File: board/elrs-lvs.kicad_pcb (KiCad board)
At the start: 4 copper layers, 46 x 22 mm, 150 parts, among them J1 PWM, J10 CF/Prog, J11 Holes, J12 Balance, J13 U.FL, J2 PWM, J3 PWM, J4 PWM, J5 PWM, J6 PWM, J7 PWM, J8 PWM, J9 Little Tower, SW1 SW_SPST, SW2 SW_SPST, U1 ESP32-PICO-V3, U2 SX1281, U3 TPSM82901SISR, U4 2450FM07D0034T, Y1 52Mhz TCXO

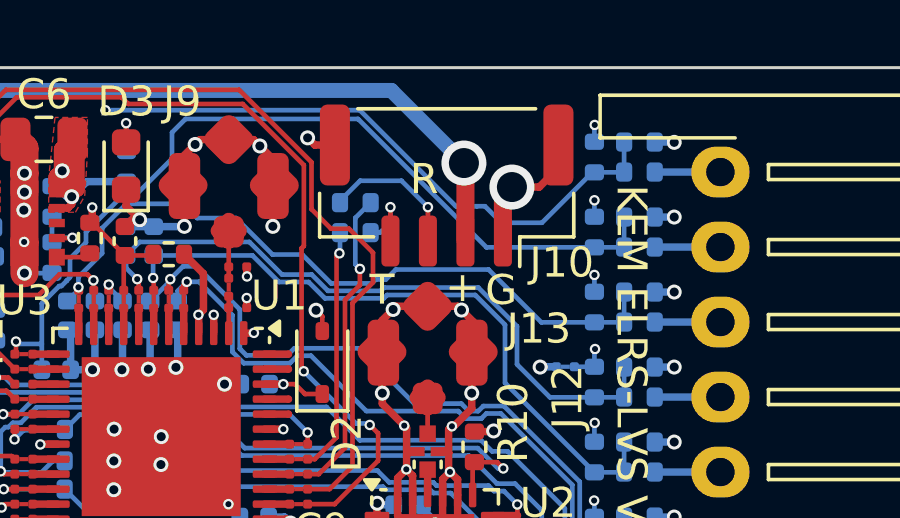
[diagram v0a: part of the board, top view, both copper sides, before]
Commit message: invert serial connector pinout
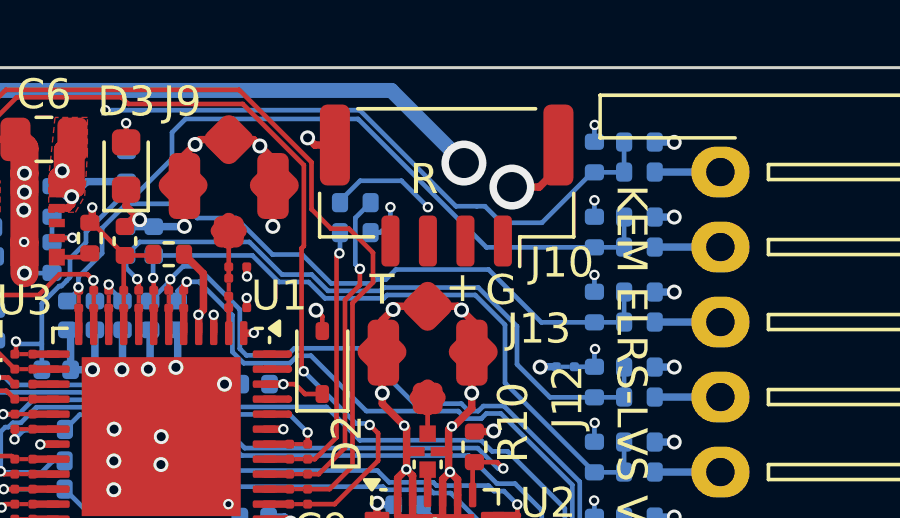
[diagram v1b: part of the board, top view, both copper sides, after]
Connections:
- J10 pad 1: GND -> Net-(J10-Pin_1)
- J10 pad 2: +5V -> Net-(J10-Pin_2)
- J10 pad 3: Net-(J10-Pin_3) -> +5V
- J10 pad 4: Net-(J10-Pin_4) -> GND
- R47 pad 1: Net-(J10-Pin_3) -> Net-(J10-Pin_2)
- R48 pad 1: Net-(J10-Pin_4) -> Net-(J10-Pin_1)
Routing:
- net Net-(J10-Pin_3): track 4.76 -> 0.00 mm, vias 1 -> 0
- net Net-(J10-Pin_2): track 0.00 -> 3.63 mm, vias 0 -> 1
- net +5V: track 150.8 -> 148.2 mm
- net Net-(J10-Pin_4): track 2.43 -> 0.00 mm, vias 1 -> 0
- net GND: track 300.4 -> 298.9 mm
- net Net-(J10-Pin_1): track 0.00 -> 1.30 mm, vias 0 -> 1

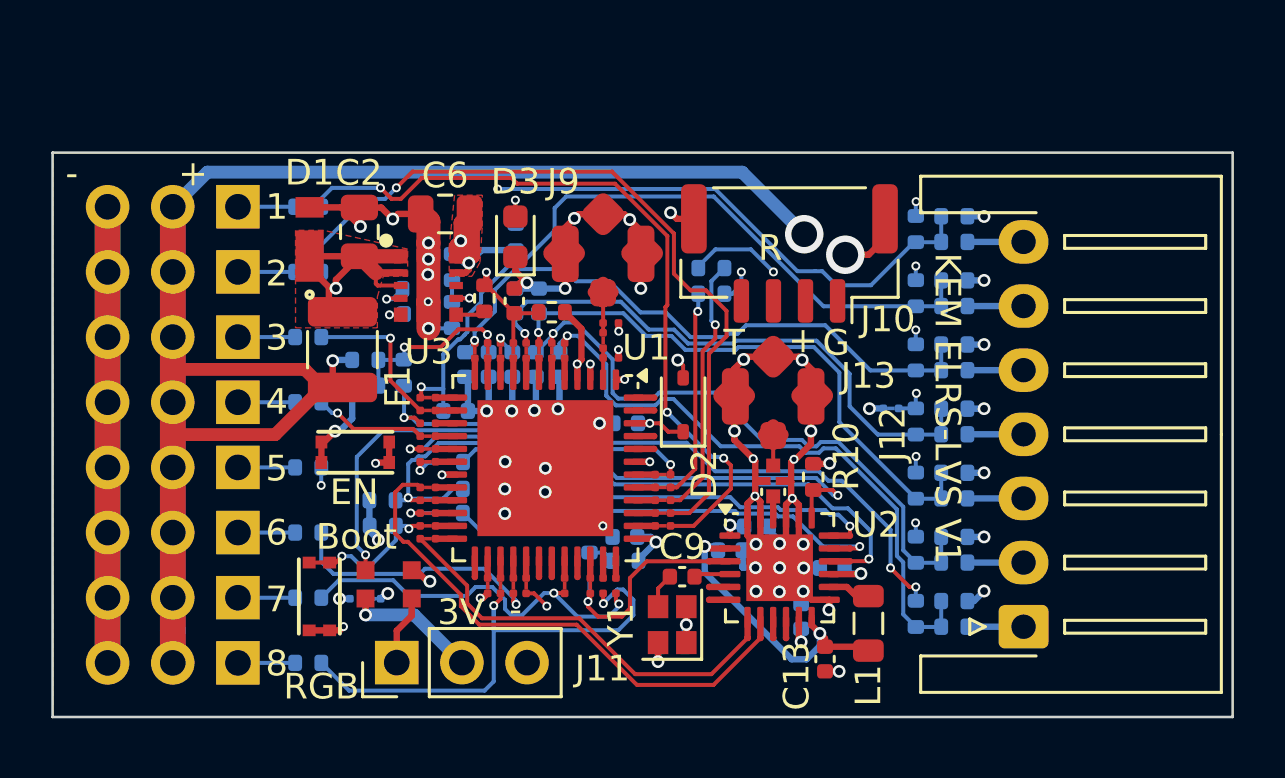
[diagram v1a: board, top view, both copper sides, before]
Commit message: remove dnp options and test points
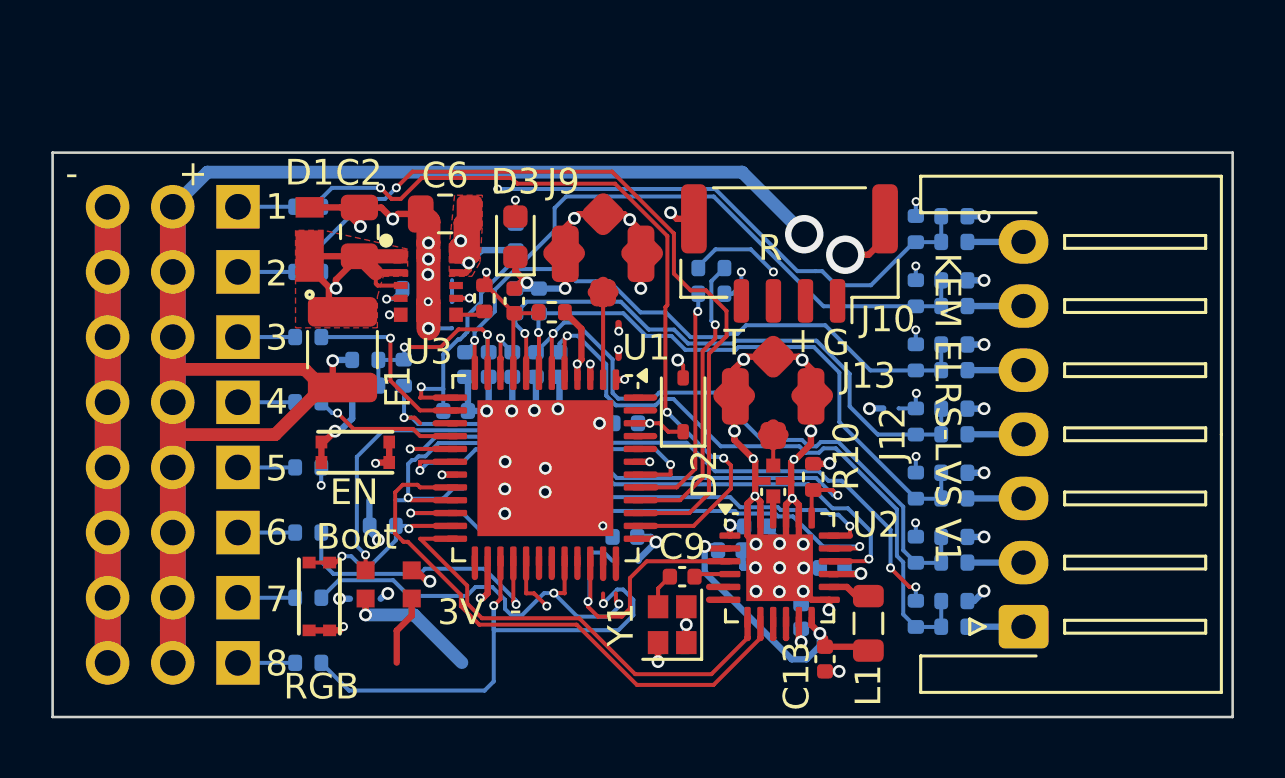
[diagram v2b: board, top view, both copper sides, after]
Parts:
- removed C22, C23: DNP, elrs-lvs:R_0201_0603_NP
- removed C5: DNP, Capacitor_SMD:C_0402_1005Metric
- removed J11: Holes, Connector_PinHeader_2.54mm:PinHeader_1x03_P2.54mm_Vertical
- removed JP1, JP12, JP13, JP14, JP15, JP16, JP17, JP18, JP19, JP2, JP20, JP21, JP22, JP23, JP25, JP26, JP27, JP29, JP3, JP31, JP32, JP33, JP34, JP35, JP36, JP4, JP41, JP5, JP7, JP8, L2: JP, elrs-lvs:R_0201_0603_JP
- removed JP24, JP28, JP30: NP, elrs-lvs:R_0201_0603_NP
- removed JP37: SolderJumper_3_Bridged12, elrs-lvs:R_0201_0603_JP_123
- removed R11, R12, R4, R5, R6, R7, R8, R9: DNP, Resistor_SMD:R_0402_1005Metric
- removed TP10, TP11, TP12, TP13, TP14, TP15, TP16, TP18, TP19, TP2, TP20, TP3, TP4, TP5, TP6, TP7, TP8, TP9: TP, elrs-lvs:TestPoint_Pad_D0.25mm
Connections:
- D4 pad 4: /LEDPWR -> +3.3V
- R31 pad 2: /VBAT_DET -> +3.3V
- R32 pad 2: /VBAT_DET -> +3.3V
- R33 pad 2: /VBAT_DET -> +3.3V
- R34 pad 2: /VBAT_DET -> +3.3V
- R35 pad 2: /VBAT_DET -> +3.3V
- R36 pad 2: /VBAT_DET -> +3.3V
- R37 pad 2: /VBAT_DET -> +3.3V
- R38 pad 2: /VBAT_DET -> +3.3V
- U1 pad 10: Net-(JP34-A) -> /LVS7
- U1 pad 11: Net-(JP35-A) -> /VS_5V
- U1 pad 12: Net-(JP32-A) -> /LVS5
- U1 pad 13: Net-(JP33-A) -> /LVS6
- U1 pad 14: Net-(JP29-A) -> /PWM3
- U1 pad 15: Net-(JP30-A) -> unconnected-(U1-IO26-Pad15)
- U1 pad 16: Net-(JP31-A) -> /PWM4
- U1 pad 17: Net-(JP22-A) -> /RADIO_NSS
- U1 pad 18: Net-(JP20-A) -> /RADIO_SCK
- U1 pad 2: Net-(U1-LNA_IN) -> Net-(J9-In)
- U1 pad 20: Net-(JP21-A) -> /RADIO_DIO1
- U1 pad 21: Net-(JP23-A) -> /RADIO_MISO
- U1 pad 22: Net-(JP14-A) -> /RADIO_MOSI
- U1 pad 23: Net-(JP12-A) -> /BOOT
- U1 pad 24: Net-(JP16-A) -> /RADIO_BUSY
- U1 pad 25: Net-(U1-IO16) -> unconnected-(U1-IO16-Pad25)
- U1 pad 26: Net-(JP36-A) -> +3.3V
- U1 pad 27: Net-(JP7-B) -> /PWM8
- U1 pad 28: Net-(JP18-A) -> /PWM6
- U1 pad 29: Net-(JP19-A) -> /PWM5
- U1 pad 30: Net-(U1-CMD) -> unconnected-(U1-CMD-Pad30)
- U1 pad 31: Net-(U1-CLK) -> unconnected-(U1-CLK-Pad31)
- U1 pad 32: Net-(JP8-B) -> /PWM7
- U1 pad 33: Net-(U1-SD1) -> unconnected-(U1-SD1-Pad33)
- U1 pad 34: Net-(JP17-A) -> /RADIO_RST
- U1 pad 35: Net-(JP24-A) -> unconnected-(U1-IO18-Pad35)
- U1 pad 36: Net-(JP28-A) -> unconnected-(U1-IO23-Pad36)
- U1 pad 38: Net-(JP25-A) -> /PWM1
- U1 pad 39: Net-(JP27-A) -> /PWM2
- U1 pad 40: Net-(JP15-A) -> /SERIAL_RX
- U1 pad 41: Net-(JP13-A) -> /SERIAL_TX
- U1 pad 42: Net-(JP26-A) -> /LED_RGB
- U1 pad 44: Net-(U1-XTAL_N_NC) -> unconnected-(U1-XTAL_N_NC-Pad44)
- U1 pad 45: Net-(U1-XTAL_P_NC) -> unconnected-(U1-XTAL_P_NC-Pad45)
- U1 pad 47: Net-(U1-CAP2_NC) -> unconnected-(U1-CAP2_NC-Pad47)
- U1 pad 48: Net-(U1-CAP1_NC) -> unconnected-(U1-CAP1_NC-Pad48)
- U1 pad 5: Net-(JP1-B) -> /LVS1
- U1 pad 6: Net-(JP2-B) -> /LVS2
- U1 pad 7: Net-(JP3-B) -> /LVS3
- U1 pad 8: Net-(JP4-B) -> /LVS4
- U1 pad 9: Net-(JP5-B) -> /RESET
- U2 pad 10: Net-(U2-DIO3) -> unconnected-(U2-DIO3-Pad10)
- U2 pad 5: Net-(TP9-Pad1) -> unconnected-(U2-GND-Pad5)
- U2 pad 6: Net-(U2-XTB) -> unconnected-(U2-XTB-Pad6)
- U2 pad 9: Net-(U2-DIO2) -> unconnected-(U2-DIO2-Pad9)
- U3 pad 5: Net-(U3-SS/TR) -> unconnected-(U3-SS/TR-Pad5)
- U3 pad 7: Net-(U3-FB) -> unconnected-(U3-FB-Pad7)
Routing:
- net +3.3V: track 98.8 -> 151.3 mm, vias 17 -> 27
- net /VBAT_DET: track 45.2 -> 0.00 mm, vias 9 -> 0
- net /LEDPWR: track 5.80 -> 0.00 mm, vias 1 -> 0
- net unconnected-(U3-FB-Pad7): track 0.00 -> 2.12 mm, vias 0 -> 1
- net Net-(U3-FB): track 2.12 -> 0.00 mm, vias 1 -> 0
- net Net-(J9-In): track 1.55 -> 3.38 mm
- net /LVS5: track 23.8 -> 25.3 mm
- net /SERIAL_RX: track 10.3 -> 11.7 mm
- net /RADIO_NSS: track 20.4 -> 21.8 mm
- net /RADIO_MOSI: track 20.3 -> 21.7 mm
- net /PWM6: track 10.1 -> 11.6 mm
- net /PWM2: track 30.4 -> 31.8 mm
- net /RADIO_SCK: track 19.9 -> 21.3 mm
- net /RESET: track 21.6 -> 23.0 mm
- net /LVS7: track 27.5 -> 28.9 mm
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
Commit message: update library footprints
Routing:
- net VIN: track 25.0 -> 11.2 mm, vias 2 -> 0
- net +3.3V: track 151.3 -> 141.8 mm, vias 27 -> 25
- net /PWM8: track 21.5 -> 12.3 mm, vias 2 -> 1
- net /PWM7: track 16.3 -> 12.6 mm, vias 2 -> 1
- net Net-(J10-Pin_2): track 3.63 -> 0.00 mm, vias 1 -> 0
- net /RADIO_RST: track 12.2 -> 9.27 mm, vias 1 -> 0
- net /RADIO_MISO: track 28.6 -> 25.8 mm
- net /RGB: track 2.74 -> 0.00 mm
- net unconnected-(U3-FB-Pad7): track 2.12 -> 0.00 mm, vias 1 -> 0
- net Net-(J10-Pin_1): track 1.30 -> 0.00 mm, vias 1 -> 0
- net unconnected-(U3-SS/TR-Pad5): track 1.01 -> 0.00 mm, vias 1 -> 0
- net unconnected-(U1-IO26-Pad15): track 0.83 -> 0.00 mm
- net unconnected-(U1-IO23-Pad36): track 0.83 -> 0.00 mm
- net unconnected-(U1-IO18-Pad35): track 0.83 -> 0.00 mm
- net unconnected-(U2-XTB-Pad6): track 0.81 -> 0.00 mm
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
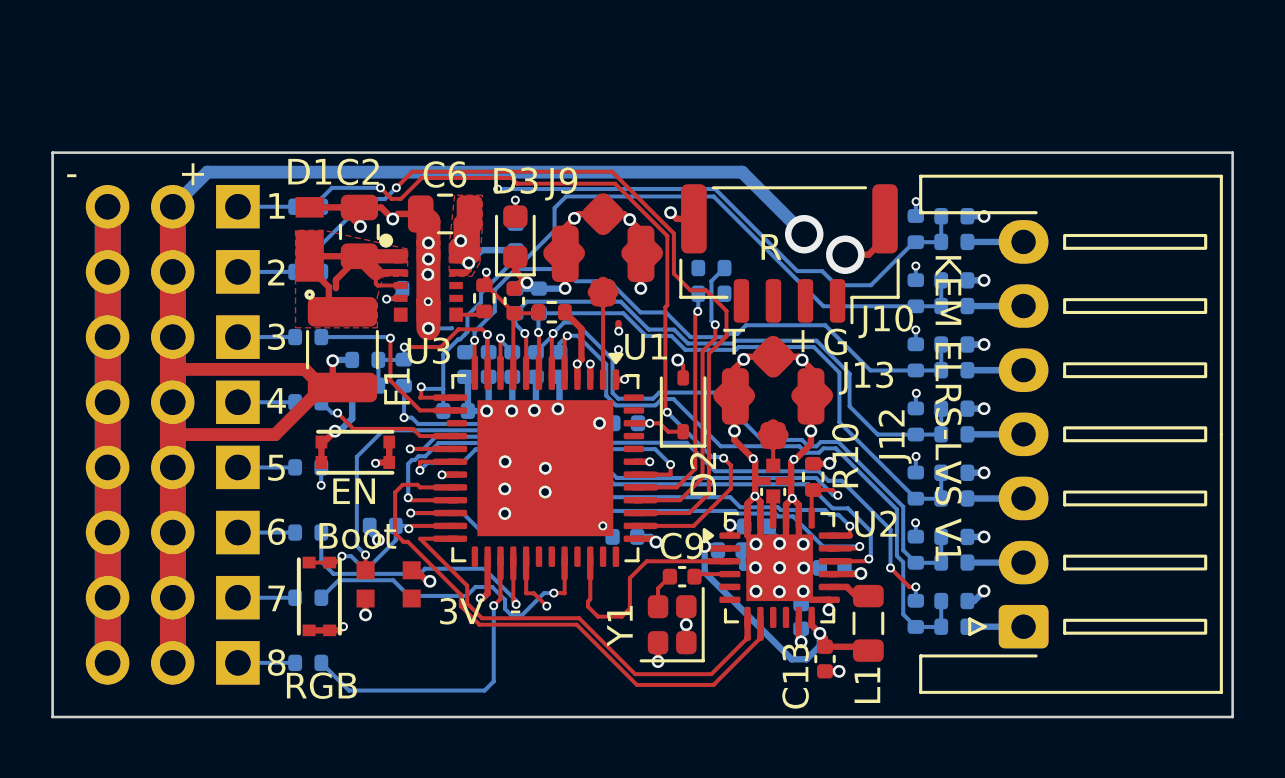
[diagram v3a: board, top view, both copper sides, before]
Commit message: initial placement for single sided lower density
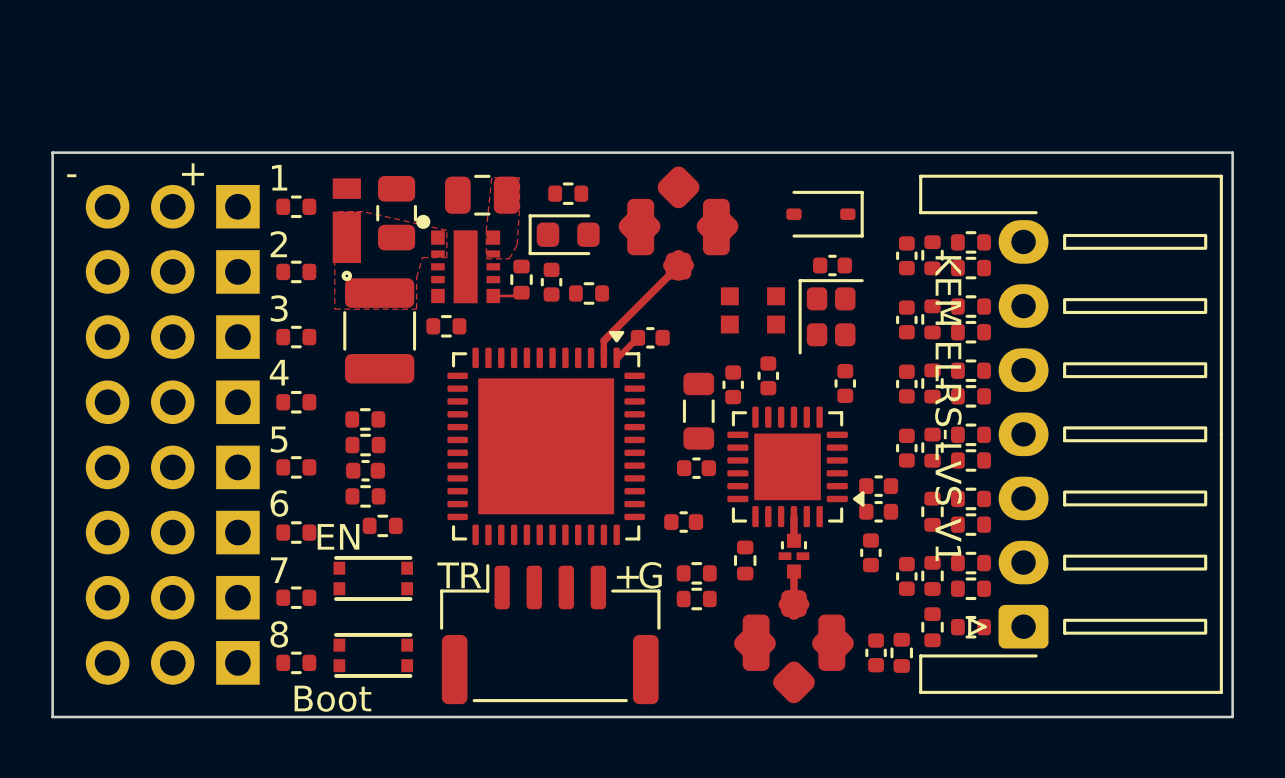
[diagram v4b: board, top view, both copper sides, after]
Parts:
- C10, C11, C12, C14, C15, C16, C17, C18, C19, C20, C21, C3, C4, C7, C8, R13, R14, R15, R16, R17, R18, R19, R2, R20, R21, R22, R23, R24, R25, R26, R27, R28, R29, R30, R31, R32, R33, R34, R35, R36, R37, R38, R39, R40, R41, R42, R43, R44, R45, R46, R47, R48: moved to F.Cu
- J12: footprint Connector_JST:JST_XH_S7B-XH-A-1_1x07_P2.50mm_Horizontal -> elrs-lvs:JST_XH_S7B-XH-A-1_1x07_P2.50mm_Horizontal_Zero_Clearance
- moved C19 17.9 mm to (33.3, 6.52), turned to -90 degrees
- moved D4 17.8 mm to (27.3, 6.15)
- moved J10 17.6 mm to (19.4, 18.8), turned to 0 degrees
- moved C18 17.2 mm to (33.3, 9.02), turned to -90 degrees
- moved C14 16.7 mm to (32.1, 19.5)
- moved C15 16.7 mm to (33.3, 16.5), turned to -90 degrees
- moved C17 16.3 mm to (33.3, 11.5)
- moved C16 16.2 mm to (31.9, 15.6), turned to 90 degrees
- moved C11 16.1 mm to (30.4, 4.40), turned to 180 degrees
- moved C20 16.0 mm to (33.3, 4.02), turned to -90 degrees
- moved Y1 13.5 mm to (30.4, 6.40), turned to -90 degrees
- moved R47 11.9 mm to (25.1, 16.4), turned to 180 degrees
- moved R48 11.9 mm to (25.1, 17.4), turned to 0 degrees
- moved C13 11.3 mm to (26.5, 9.05)
- moved L1 10.6 mm to (25.2, 10.1), turned to -90 degrees
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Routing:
- net GND: track 298.9 -> 0.00 mm, vias 58 -> 0
- net +5V: track 148.1 -> 0.00 mm, vias 2 -> 0
- net +3.3V: track 141.8 -> 1.15 mm, vias 25 -> 0
- net /PWM2: track 31.8 -> 0.00 mm, vias 1 -> 0
- net /PWM1: track 31.0 -> 0.00 mm, vias 3 -> 0
- net /LVS6: track 30.8 -> 0.00 mm, vias 1 -> 0
- net /LVS7: track 28.8 -> 0.00 mm, vias 2 -> 0
- net /LVS1: track 26.1 -> 0.00 mm, vias 1 -> 0
- net /RADIO_MISO: track 25.8 -> 0.00 mm, vias 2 -> 0
- net /LVS5: track 25.2 -> 0.00 mm, vias 1 -> 0
- net /LVS2: track 25.1 -> 0.00 mm, vias 1 -> 0
- net /LVS4: track 23.5 -> 0.00 mm, vias 1 -> 0
- net /LVS3: track 23.5 -> 0.00 mm, vias 1 -> 0
- net /RESET: track 23.0 -> 0.00 mm, vias 2 -> 0
- net /RADIO_DIO1: track 22.7 -> 0.00 mm
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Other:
- board text removed: "3V"
- board text removed: "D"
- board text removed: "RGB"

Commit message: routing prior to starting over with rotation
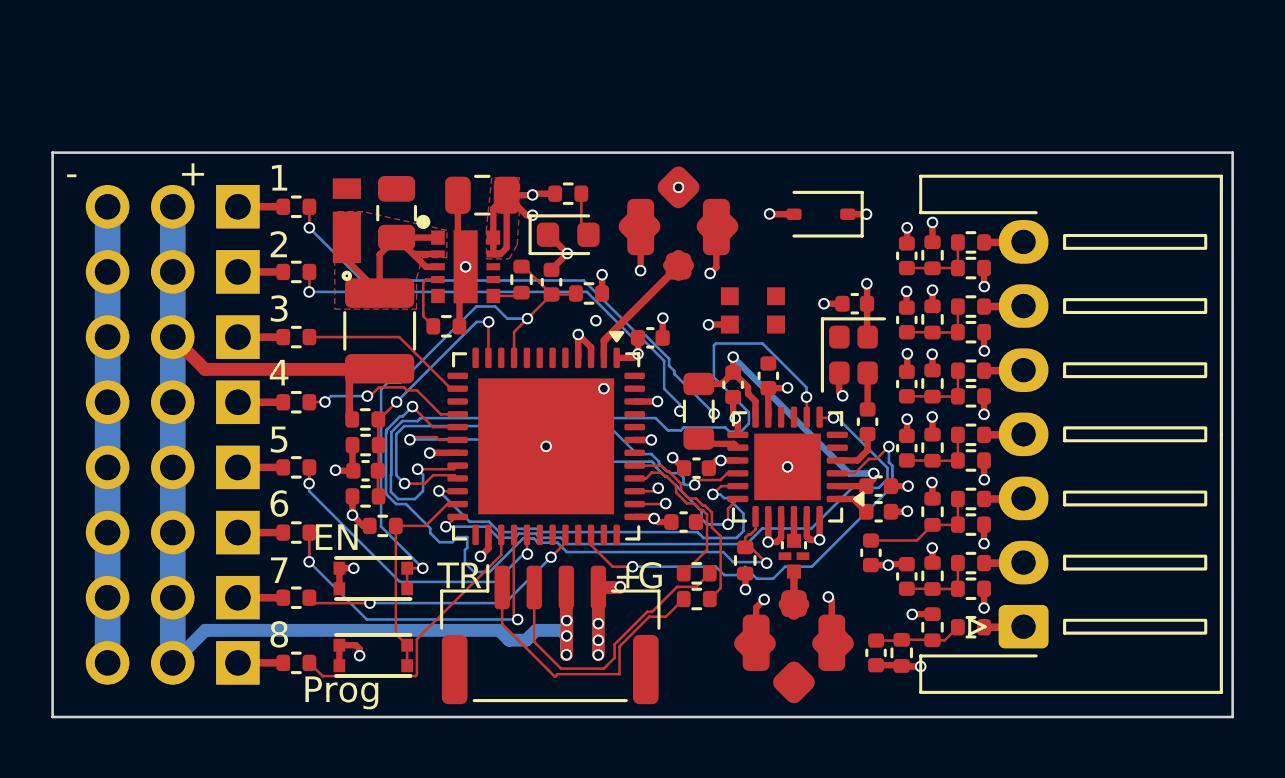
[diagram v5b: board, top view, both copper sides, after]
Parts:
- moved C9 1.73 mm to (31.8, 10.5)
- moved C11 1.73 mm to (31.3, 5.89)
- moved Y1 1.73 mm to (31.2, 7.89)
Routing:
- net GND: track 0.00 -> 211.2 mm, vias 0 -> 40
- net +3.3V: track 1.15 -> 125.6 mm, vias 0 -> 24
- net +5V: track 0.00 -> 48.4 mm, vias 0 -> 3
- net /RADIO_DIO1: track 0.00 -> 30.1 mm, vias 0 -> 2
- net /RADIO_NSS: track 0.00 -> 26.5 mm, vias 0 -> 2
- net /PWM1: track 0.00 -> 25.8 mm, vias 0 -> 3
- net /RADIO_BUSY: track 0.00 -> 23.2 mm, vias 0 -> 2
- net /PWM2: track 0.00 -> 22.3 mm, vias 0 -> 3
- net /RESET: track 0.00 -> 22.0 mm, vias 0 -> 2
- net /RADIO_MISO: track 0.00 -> 19.1 mm, vias 0 -> 2
- net /RADIO_RST: track 0.00 -> 18.5 mm, vias 0 -> 2
- net /RADIO_SCK: track 0.00 -> 17.1 mm, vias 0 -> 2
- net /RADIO_MOSI: track 0.00 -> 16.9 mm, vias 0 -> 2
- net /PWM6: track 0.00 -> 13.6 mm, vias 0 -> 2
- net /V_DCC: track 0.00 -> 13.3 mm, vias 0 -> 2
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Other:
- board text added: "KEM ELRS-LVS V2"
- board text added: "Prog"
- board text removed: "Boot"
- board text removed: "KEM ELRS-LVS V1"
